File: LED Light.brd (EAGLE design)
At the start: 101.6 x 40.6 mm, 13 parts, among them J1 AVR_SPI_PRG_6NS, U1 Tiny85-20-SMT

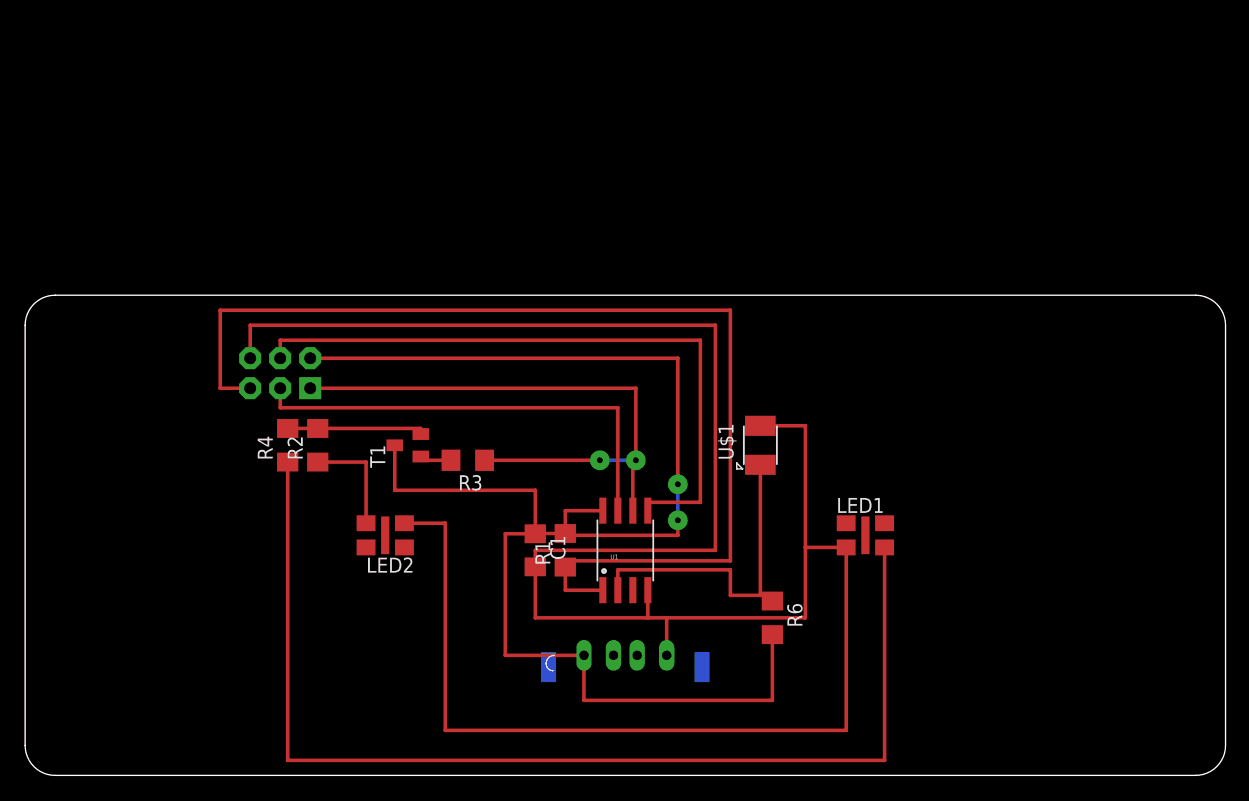
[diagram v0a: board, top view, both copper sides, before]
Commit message: Board w/ accelerometer and LiPo charging circuit.
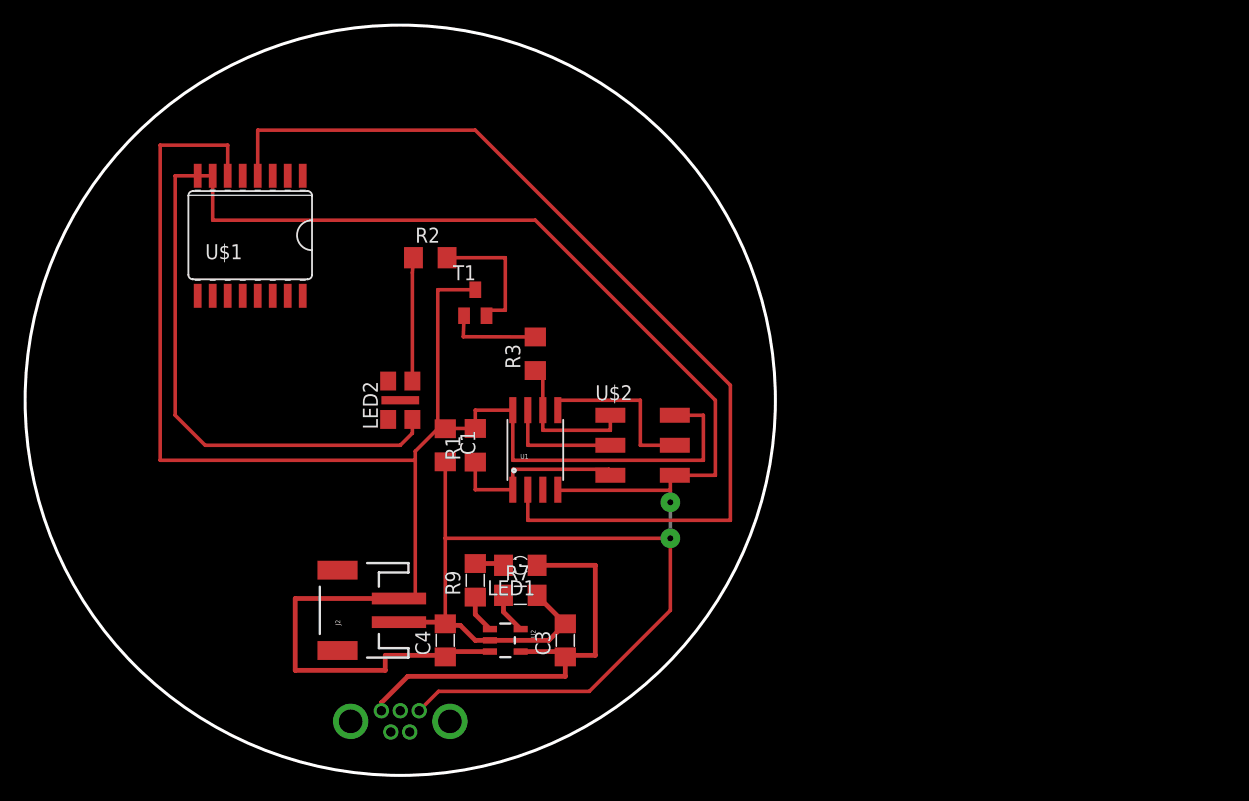
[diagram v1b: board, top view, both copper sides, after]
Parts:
- removed J1: AVR_SPI_PRG_6NS, SparkFun-Connectors:2X3-NS
- removed R4: (no value), rcl:R1206
- removed R6: 49.9K, rcl:R1206
- added C3, C4: 4.7uF, cellphone-rcl:C1206
- added J2: (no value), SparkFun-Connectors:JST-2-SMD
- added R7: 2K, cellphone-rcl:R1206
- added R9: 470, cellphone-rcl:R1206
- added U$2: AVRISPSMD, fab:2X03SMD
- added U2: MCP73831, SparkFun:SOT23-5
- JP1: value USB_A_VERTICAL -> USB-B-VERTICAL; device LED Light:USB_A_VERTICAL -> LED Light:USB_MINIB_VERTICAL
- LED1: value ML-EFAB -> (none); device LED Light:ML-E-FAB -> cellphone-led:1206
- U$1: value PHOTOTRANSISTOR-NPN-OP580AD -> MMA1270KEG; device LED Light:OP580DA -> LED Light:SOIC16
- moved U$1 47.9 mm to (17.8, 45.7), turned to 180 degrees
- moved LED1 29.3 mm to (41.9, 17.8), turned to 180 degrees
- moved JP1 19.9 mm to (31.8, 4.57), turned to 90 degrees
- moved R2 18.5 mm to (34.3, 43.8), turned to 0 degrees
- moved T1 13.4 mm to (38.1, 40.0), turned to 0 degrees
- moved C1 11.7 mm to (35.6, 27.9)
- moved R1 11.7 mm to (38.1, 27.9)
- moved LED2 11.5 mm to (31.8, 31.8), turned to 90 degrees
- moved U1 11.4 mm to (43.2, 27.6)
- moved R3 10.7 mm to (43.2, 35.7), turned to 90 degrees
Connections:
- removed net N$5: LED1.A@1, R4.1
- new net N$35: R9.1, U2.1
- new net N$36: LED1.C, R9.2
- new net PROG: R7.1, U2.5
- new net VUSB: C3.1, JP1.VBUS, LED1.A, U2.4
- net GND: now also C3.2, C4.2, J2.1, R7.2, U$1.7, U$1.8, U$2.6, U2.2; no longer J1.6, LED1.C@1, U$1.EMITTER
- net MISO: now also U$2.1; no longer J1.1
- net MOSI: now also U$2.4; no longer J1.4
- net N$1: no longer R4.2
- net N$7: now also U$1.4; no longer R6.1, U$1.COLLECTOR
- net RESET: now also U$2.5; no longer J1.5
- net SCK: now also U$2.3; no longer J1.3
- net VCC: now also C4.1, J2.2, U$1.6, U$2.2, U2.3; no longer J1.2, JP1.VBUS, R6.2
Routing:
- net N$5: track 93.8 -> 0.00 mm
- net RESET: track 93.2 -> 16.0 mm
- net N$7: track 28.5 -> 84.0 mm
- net MOSI: track 56.0 -> 14.6 mm
- net MISO: track 51.0 -> 12.7 mm, vias 2 -> 0
- net VUSB: track 0.00 -> 38.0 mm
- net SCK: track 38.9 -> 9.96 mm
- net VCC: track 127.6 -> 155.6 mm, vias 2 -> 0
- net N$2: track 2.88 -> 7.88 mm
- net PROG: track 0.00 -> 3.46 mm
- net N$35: track 0.00 -> 3.22 mm
- net N$36: track 0.00 -> 2.54 mm
- net GND: track 204.5 -> 206.4 mm, vias 0 -> 2
- net N$3: track 9.26 -> 10.4 mm
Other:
- board size 101.6 x 40.6 mm -> 63.5 x 63.5 mm

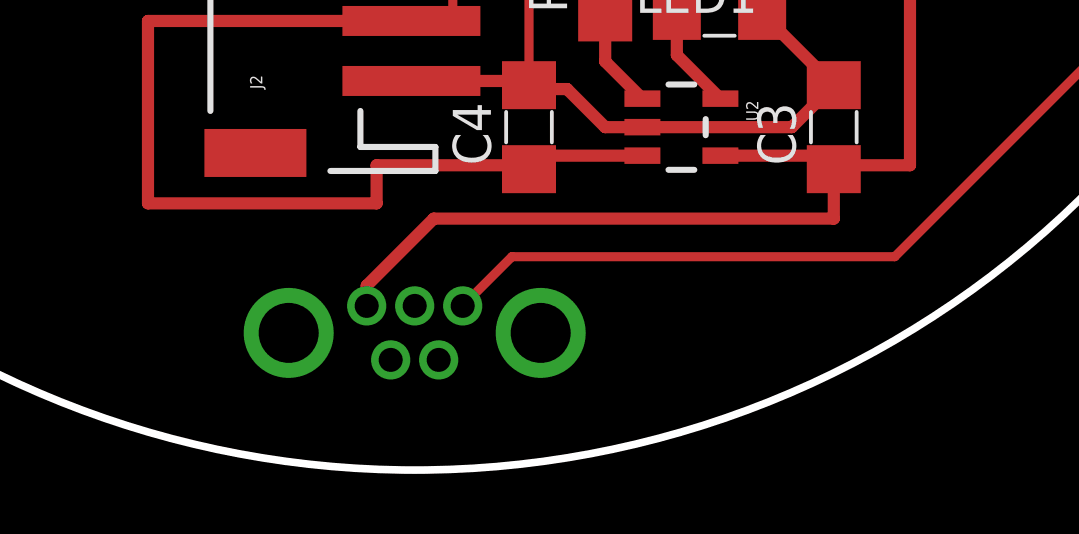
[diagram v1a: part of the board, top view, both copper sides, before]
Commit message: Un-mirror USB connector.
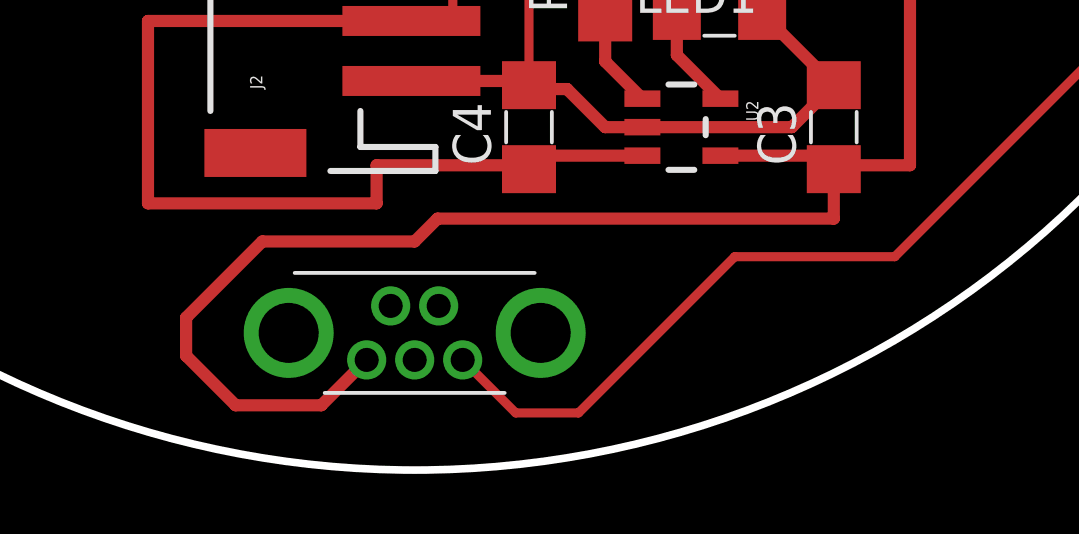
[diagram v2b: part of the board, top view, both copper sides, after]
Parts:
- flipped JP1 to the top, turned to 270 degrees
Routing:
- net VUSB: track 38.0 -> 52.4 mm
- net GND: track 206.4 -> 208.6 mm
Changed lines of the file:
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@@
 <element name="R1" library="rcl" package="R1206" value="10K" x="38.1" y="27.94" rot="R90"/>
 <element name="R2" library="rcl" package="R1206" value="" x="34.29" y="43.815"/>
-<element name="JP1" library="LED Light" package="USB_MINIB_VERTICAL" value="USB-B-VERTICAL" x="31.75" y="4.572" rot="MR90"/>
+<element name="JP1" library="LED Light" package="USB_MINIB_VERTICAL" value="USB-B-VERTICAL" x="31.75" y="4.572" rot="R270"/>
 <element name="C1" library="rcl" package="C1206" value="1.0uF" x="35.56" y="27.94" rot="R270"/>
 <element name="LED2" library="LED Light" package="ML-E-FAB" value="ML-EFAB" x="31.75" y="31.75" rot="R90"/>
@@
 <wire x1="44.32" y1="11.43" x2="45.72" y2="12.83" width="0.4064" layer="1"/>
 <wire x1="35.56" y1="20.066" x2="35.56" y2="12.83" width="0.3048" layer="1"/>
-<wire x1="34.99" y1="7.112" x2="47.752" y2="7.112" width="0.3048" layer="1"/>
 <wire x1="47.752" y1="7.112" x2="54.61" y2="13.97" width="0.3048" layer="1"/>
-<wire x1="33.35" y1="5.472" x2="34.99" y2="7.112" width="0.3048" layer="1"/>
 <wire x1="14.605" y1="50.7492" x2="15.875" y2="50.7492" width="0.3048" layer="1"/>
 <wire x1="12.7" y1="30.48" x2="12.7" y2="50.7492" width="0.3048" layer="1"/>
@@
 <wire x1="31.75" y1="27.94" x2="15.24" y2="27.94" width="0.3048" layer="1"/>
 <wire x1="15.24" y1="27.94" x2="12.7" y2="30.48" width="0.3048" layer="1"/>
+<wire x1="47.752" y1="7.112" x2="42.418" y2="7.112" width="0.3048" layer="1"/>
+<wire x1="42.418" y1="7.112" x2="37.211" y2="1.905" width="0.3048" layer="1"/>
+<wire x1="37.211" y1="1.905" x2="35.117" y2="1.905" width="0.3048" layer="1"/>
+<wire x1="35.117" y1="1.905" x2="33.35" y2="3.672" width="0.3048" layer="1"/>
 </signal>
 <signal name="RESET">
@@
 <wire x1="48.26" y1="10.16" x2="45.72" y2="10.16" width="0.4064" layer="1"/>
 <wire x1="45.72" y1="10.16" x2="45.72" y2="10.03" width="0.4064" layer="1"/>
-<wire x1="30.15" y1="5.472" x2="30.15" y2="6.147" width="0.4064" layer="1"/>
-<wire x1="30.15" y1="6.147" x2="32.385" y2="8.382" width="0.4064" layer="1"/>
-<wire x1="32.385" y1="8.382" x2="45.72" y2="8.382" width="0.4064" layer="1"/>
 <wire x1="45.72" y1="8.382" x2="45.72" y2="10.03" width="0.4064" layer="1"/>
+<wire x1="45.72" y1="8.382" x2="32.512" y2="8.382" width="0.4064" layer="1"/>
+<wire x1="32.512" y1="8.382" x2="31.75" y2="7.62" width="0.4064" layer="1"/>
+<wire x1="31.75" y1="7.62" x2="26.67" y2="7.62" width="0.4064" layer="1"/>
+<wire x1="26.67" y1="7.62" x2="24.13" y2="5.08" width="0.4064" layer="1"/>
+<wire x1="24.13" y1="5.08" x2="24.13" y2="3.81" width="0.4064" layer="1"/>
+<wire x1="24.13" y1="3.81" x2="25.781" y2="2.159" width="0.4064" layer="1"/>
+<wire x1="25.781" y1="2.159" x2="28.637" y2="2.159" width="0.4064" layer="1"/>
+<wire x1="28.637" y1="2.159" x2="30.15" y2="3.672" width="0.4064" layer="1"/>
 </signal>
 <signal name="N$35">

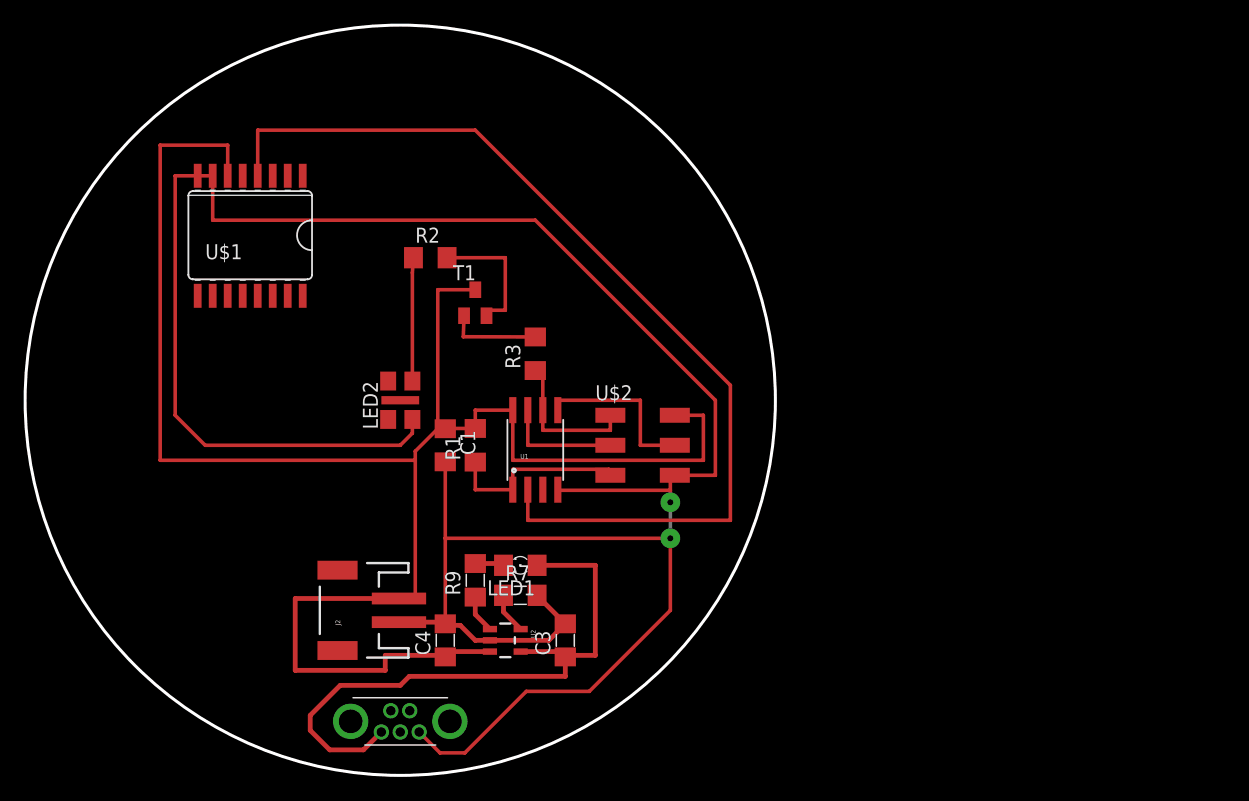
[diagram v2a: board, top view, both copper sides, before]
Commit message: Replace non-standard parts, two-sided layout, silk
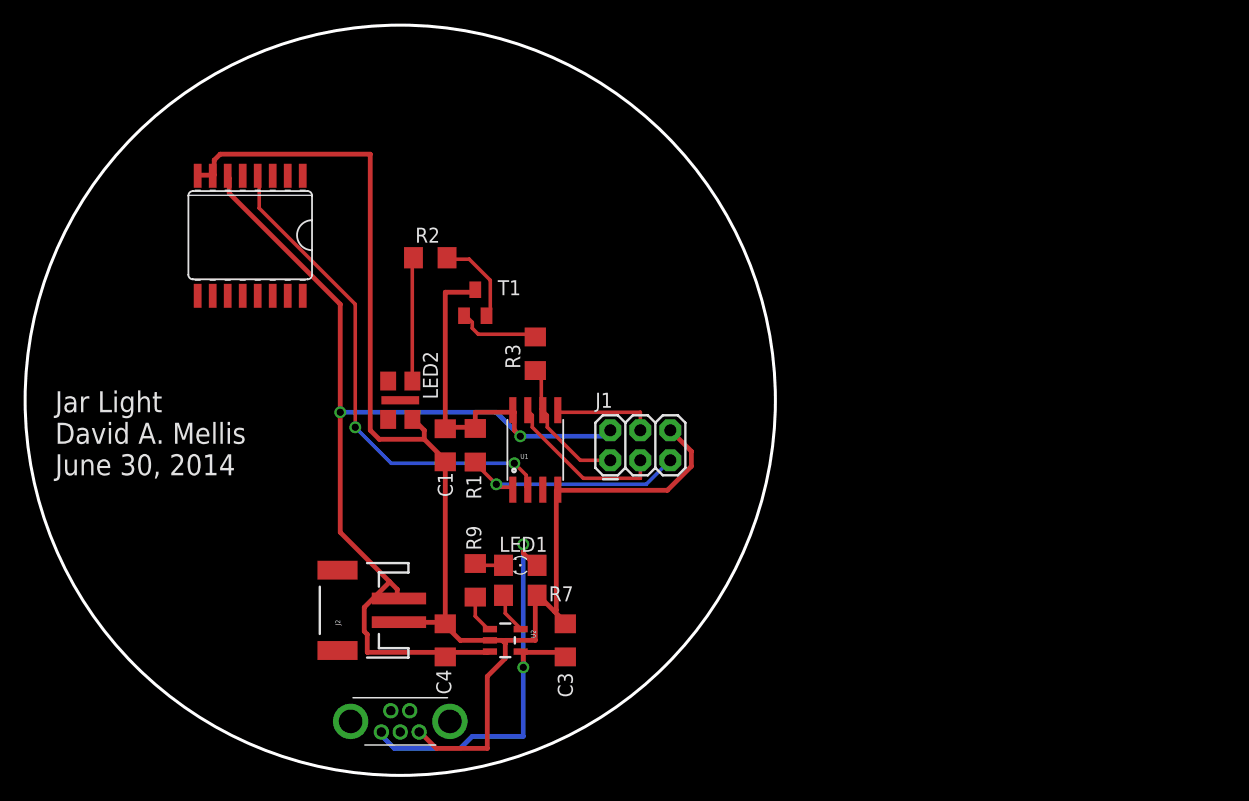
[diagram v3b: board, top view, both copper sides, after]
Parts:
- removed U$2: AVRISPSMD, fab:2X03SMD
- added J1: AVR_SPI_PRG_6PTH, SparkFun-Connectors:2X3
- C3, C4: device cellphone-rcl:C1206 -> rcl:C1206
- R2: value (none) -> 10
- R7, R9: device cellphone-rcl:R1206 -> rcl:R1206
- U2: device SparkFun:SOT23-5 -> SparkFun-PowerIC:SOT23-5
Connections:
- net GND: now also J1.6; no longer U$2.6
- net MISO: now also J1.1; no longer U$2.1
- net MOSI: now also J1.4; no longer U$2.4
- net RESET: now also J1.5; no longer U$2.5
- net SCK: now also J1.3; no longer U$2.3
- net VCC: now also J1.2; no longer U$2.2
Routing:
- net GND: track 208.6 -> 125.0 mm, vias 2 -> 0
- net VCC: track 155.6 -> 107.6 mm, vias 0 -> 2
- net N$7: track 84.0 -> 42.1 mm, vias 0 -> 2
- net VUSB: track 52.4 -> 37.4 mm, vias 0 -> 2
- net MOSI: track 14.6 -> 8.60 mm
- net SCK: track 9.96 -> 14.1 mm
- net N$1: track 11.4 -> 7.58 mm
- net RESET: track 16.0 -> 19.8 mm, vias 0 -> 1
- net MISO: track 12.7 -> 11.7 mm
- net N$2: track 7.88 -> 7.19 mm
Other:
- board text added: "Jar Light David A. Mellis June 30, 2014"
